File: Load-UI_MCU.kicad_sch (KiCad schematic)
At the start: 34 parts, among them IC1 MSPM0G3519SPMR, IC2 TPS73533DRVT, J1 Conn_01x05_Socket, J10 Conn_01x02_Socket, J11 Conn_01x02_Socket, J15 Conn_01x08_Pin, J8 Conn_01x06_Socket, SW1 SW_Push, SW2 SW_Push, SW3 SW_Push_DPDT

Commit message: schematic comments
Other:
- note added: "Latch button so we can control whether the hand made or module converter will be used."
- note added: "To use higher voltages on gate driver and digital pot"
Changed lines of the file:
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@@
+		)
+	)
+	(arc
+		(start 171.45 16.51)
+		(mid 172.2699 13.6123)
+		(end 175.26 13.97)
+		(stroke
+			(width 0)
+			(type default)
+		)
+		(fill
+			(type none)
+		)
+	)
+	(text "To use higher voltages on gate driver and digital pot"
+		(exclude_from_sim no)
+		(at 201.93 14.224 0)
+		(effects
+			(font
+				(size 1.27 1.27)
+			)
 		)
 	)
@@
 		(exclude_from_sim no)
 		(at 200.152 89.916 0)
+		(effects
+			(font
+				(size 1.27 1.27)
+			)
+		)
+	)
+	(text "Latch button so we can control whether\nthe hand made or module converter will\nbe used."
+		(exclude_from_sim no)
+		(at 34.036 113.792 0)
 		(effects
 			(font
@@
 		)
 	)
+	(polyline
+		(pts
+			(xy 175.26 12.7) (xy 175.26 13.97)
+		)
+		(stroke
+			(width 0)
+			(type default)
+		)
+	)
 	(wire
 		(pts
@@
 		)
 	)
-	(polyline
-		(pts
-			(xy 12.7 97.79) (xy 12.7 119.38)
-		)
-		(stroke
-			(width 0)
-			(type default)
-		)
-	)
 	(wire
 		(pts
@@
 		)
 		(stroke
+			(width 0)
+			(type default)
+		)
+	)
+	(polyline
+		(pts
+			(xy 173.99 13.97) (xy 175.26 13.97)
+		)
+		(stroke

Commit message: Last update after PR4, mostly done I need revisions from rest of members with special attention on grounding layout
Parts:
- removed D5: LED, LED_SMD:LED_0805_2012Metric_Pad1.15x1.40mm_HandSolder, symbol Device:LED
- removed R16: 1k, Resistor_SMD:R_1206_3216Metric_Pad1.30x1.75mm_HandSolder, symbol Device:R
- removed SW3: SW_Push_DPDT, Latch_PB:SW_DPDT_XLX, symbol Switch:SW_Push_DPDT
- R8, R9: value 47k -> 1k
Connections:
- net SCL: now reaches IC1.60 (PB8)
- net SDA: now reaches IC1.61 (PB9)
- net Load/POT_MISO renamed Load/ConverterOUT_MISO
- net Load/POT_MOSI renamed Load/ConverterOUT_MOSI
- net Load/POT_SCK renamed Load/ConverterOUT_SCLK
- no-connect marks 16 -> 11
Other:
- sheet Load ports: added POT_SCL, POT_SDA, SELECT_CONVERTER; removed POT_CS, POT_MISO, POT_MOSI, POT_SCK
- note added: "I2C0"
- note added: "SPI0"
- note removed: "Latch button so we can control whether the hand made or module converter will be used."
- note removed: "SPI0 for both INA229"
- note removed: "SPI2"

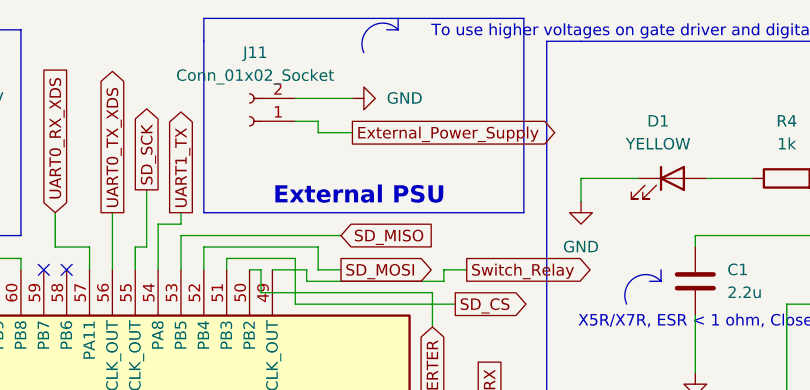
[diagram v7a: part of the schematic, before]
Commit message: added two more testpoints
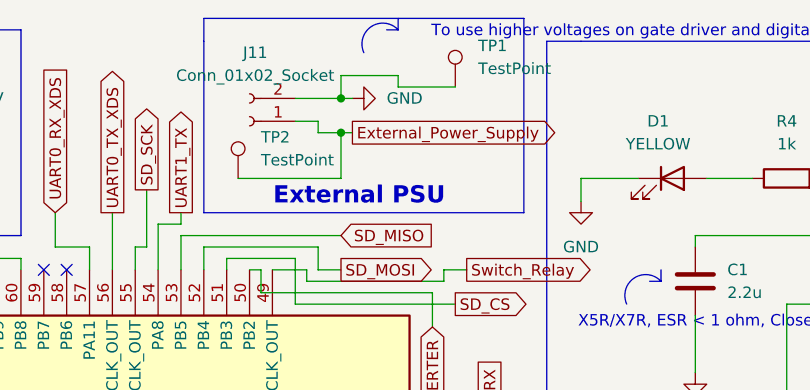
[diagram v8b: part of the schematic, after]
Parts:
- added TP1, TP2: TestPoint, TestPoint:TestPoint_Pad_D1.0mm, symbol Connector:TestPoint
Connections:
- net External_Power_Supply: now also TP2.1
- net GND: now also TP1.1
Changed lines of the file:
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@@
 	)
 	(junction
+		(at 168.91 25.4)
+		(diameter 0)
+		(color 0 0 0 0)
+	)
+	(junction
 		(at 189.23 125.73)
 		(diameter 0)
@@
 	)
 	(junction
+		(at 168.91 21.59)
+		(diameter 0)
+		(color 0 0 0 0)
+	)
+	(junction
 		(at 34.29 82.55)
 		(diameter 0)
@@
 	(wire
 		(pts
+			(xy 157.48 30.48) (xy 168.91 30.48)
+		)
+		(stroke
+			(width 0)
+			(type default)
+		)
+	)
+	(wire
+		(pts
 			(xy 251.46 144.78) (xy 251.46 142.24)
 		)
@@
 	(wire
 		(pts
+			(xy 175.26 20.32) (xy 175.26 19.05)
+		)
+		(stroke
+			(width 0)
+			(type default)
+		)
+	)
+	(wire
+		(pts
 			(xy 27.94 59.69) (xy 27.94 57.15)
 		)
@@
 	(wire
 		(pts
-			(xy 163.83 21.59) (xy 170.18 21.59)
+			(xy 175.26 19.05) (xy 168.91 19.05)
+		)
+		(stroke
+			(width 0)
+			(type default)
+		)
+	)
+	(wire
+		(pts
+			(xy 163.83 21.59) (xy 168.91 21.59)
 		)
 		(stroke
@@
 	(wire
 		(pts
-			(xy 170.18 25.4) (xy 166.37 25.4)
+			(xy 170.18 25.4) (xy 168.91 25.4)
 		)
 		(stroke
@@
 	(wire
 		(pts
+			(xy 168.91 30.48) (xy 168.91 25.4)
+		)
+		(stroke
+			(width 0)
+			(type default)
+		)
+	)
+	(wire
+		(pts
 			(xy 204.47 86.36) (xy 204.47 96.52)
 		)
@@
 		)
 	)
+	(wire
+		(pts
+			(xy 168.91 19.05) (xy 168.91 21.59)
+		)
+		(stroke
+			(width 0)
+			(type default)
+		)
+	)
 	(polyline
 		(pts
@@
 	(wire
 		(pts
+			(xy 168.91 21.59) (xy 170.18 21.59)
+		)
+		(stroke
+			(width 0)
+			(type default)
+		)
+	)
+	(wire
+		(pts
 			(xy 31.75 87.63) (xy 36.83 87.63)
 		)
@@
 	(wire
 		(pts
+			(xy 181.61 20.32) (xy 175.26 20.32)
+		)
+		(stroke
+			(width 0)
+			(type default)
+		)
+	)
+	(wire
+		(pts
 			(xy 228.6 36.83) (xy 228.6 41.91)
 		)
@@
 	(wire
 		(pts
+			(xy 168.91 25.4) (xy 166.37 25.4)
+		)
+		(stroke
+			(width 0)
+			(type default)
+		)
+	)
+	(wire
+		(pts
 			(xy 163.83 44.45) (xy 181.61 44.45)
 		)
@@
 	)
 	(symbol
+		(lib_id "Connector:TestPoint")
+		(at 181.61 20.32 0)
+		(unit 1)
+		(exclude_from_sim no)
+		(in_bom yes)
+		(on_board yes)
+		(dnp no)
+		(fields_autoplaced yes)
+		(property "Reference" "TP1"
+			(at 184.15 15.7479 0)
+			(effects
+				(font
+					(size 1.27 1.27)
+				)
+				(justify left)
+			)
+		)
+		(property "Value" "TestPoint"
+			(at 184.15 18.2879 0)
+			(effects
+				(font
+					(size 1.27 1.27)
+				)
+				(justify left)
+			)
+		)
+		(property "Footprint" "TestPoint:TestPoint_Pad_D1.0mm"
+			(at 186.69 20.32 0)
+			(effects
+				(font
+					(size 1.27 1.27)
+				)
+				(hide yes)
+			)
+		)
+		(property "Datasheet" "~"
+			(at 186.69 20.32 0)
+			(effects
+				(font
+					(size 1.27 1.27)
+				)
+				(hide yes)
+			)
+		)
+		(property "Description" "test point"
+			(at 181.61 20.32 0)
+			(effects
+				(font
+					(size 1.27 1.27)
+				)
+				(hide yes)
+			)
+		)
+		(pin "1"
+		)
+		(instances
+			(project ""
+				(path "/526b8b14-d04c-43b9-8d25-bcbd5ccf5c4d"
+					(reference "TP1")
+					(unit 1)
+				)
+			)
+		)
+	)
+	(symbol
 		(lib_id "power:+3.3V")
 		(at 129.54 171.45 0)
@@
 					(unit 1)
 				)
+			)
+		)
+	)
+	(symbol
+		(lib_id "Connector:TestPoint")
+		(at 157.48 30.48 0)
+		(unit 1)
+		(exclude_from_sim no)
+		(in_bom yes)
+		(on_board yes)
+		(dnp no)
+		(fields_autoplaced yes)
+		(property "Reference" "TP2"
+			(at 160.02 25.9079 0)
+			(effects
+				(font
+					(size 1.27 1.27)
+				)
+				(justify left)
+			)
+		)
+		(property "Value" "TestPoint"
+			(at 160.02 28.4479 0)
+			(effects
+				(font
+					(size 1.27 1.27)
+				)
+				(justify left)
+			)
+		)
+		(property "Footprint" "TestPoint:TestPoint_Pad_D1.0mm"
+			(at 162.56 30.48 0)
+			(effects
+				(font
+					(size 1.27 1.27)
+				)
+				(hide yes)
+			)
+		)
+		(property "Datasheet" "~"
+			(at 162.56 30.48 0)
+			(effects
+				(font
+					(size 1.27 1.27)
+				)
+				(hide yes)
+			)
+		)
+		(property "Description" "test point"
+			(at 157.48 30.48 0)
+			(effects
+				(font
+					(size 1.27 1.27)
+				)
+				(hide yes)
+			)
+		)
+		(pin "1"
+		)
+		(instances
+			(project "Load-UI_MCU"
+				(path "/526b8b14-d04c-43b9-8d25-bcbd5ccf5c4d"
+					(reference "TP2")
+					(unit 1)
+				)
